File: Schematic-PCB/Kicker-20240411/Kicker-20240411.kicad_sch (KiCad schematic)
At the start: 21 parts, among them J1 Conn_01x02_Pin, J2 Conn_01x05_Pin, J3 Conn_01x02_Pin, Q1 NMOS, Q2 NMOS, U1 TSSP58P38, U2 TSSP58P38

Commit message: MD基板とキッカー基板を編集した
接続方法をピンヘッダ&ピンソケットに変更してみた
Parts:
- J2: footprint Connector_JST:JST_XH_S5B-XH-A-1_1x05_P2.50mm_Horizontal -> Connector_PinHeader_2.54mm:PinHeader_1x05_P2.54mm_Horizontal
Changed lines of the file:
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@@
 			)
 		)
-		(property "Footprint" "Connector_JST:JST_XH_S5B-XH-A-1_1x05_P2.50mm_Horizontal"
+		(property "Footprint" "Connector_PinHeader_2.54mm:PinHeader_1x05_P2.54mm_Horizontal"
 			(at 72.39 88.9 0)
 			(effects

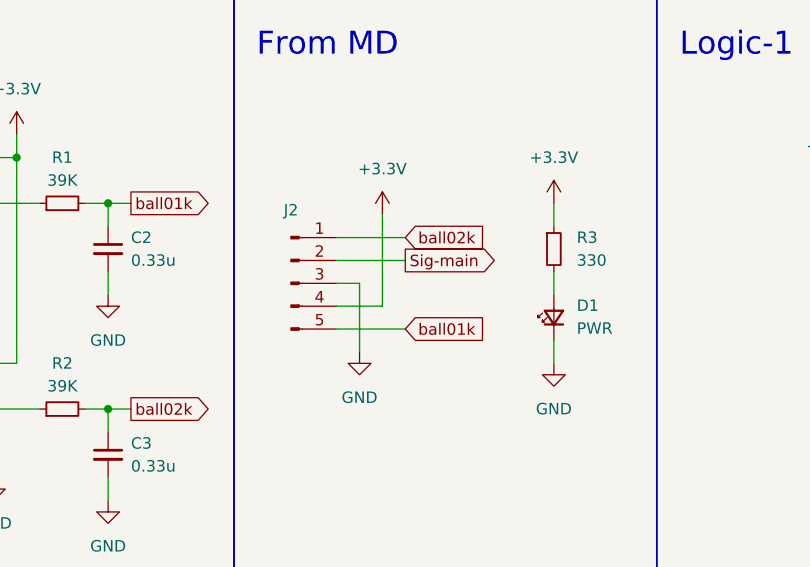
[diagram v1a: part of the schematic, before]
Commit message: 基板関連を編集した
MDとキッカーの融合基板のプロジェクト作成したから続きやっといてもらえるとありがたい
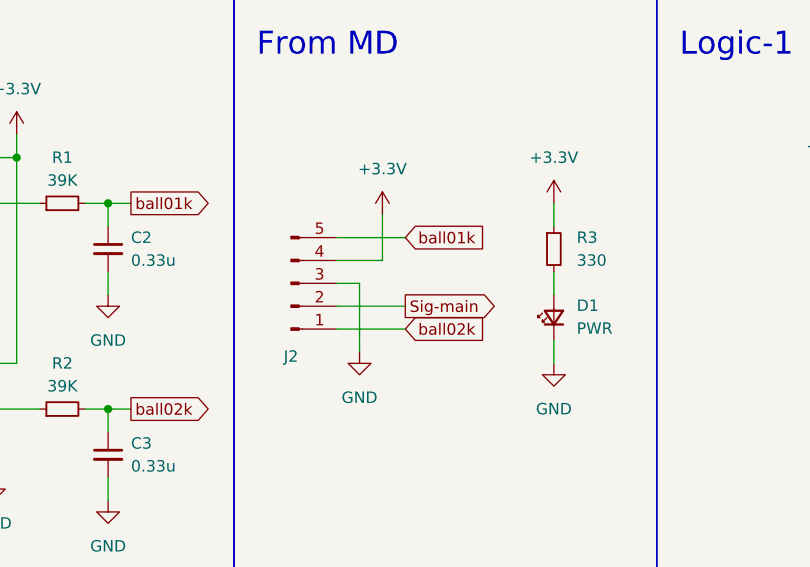
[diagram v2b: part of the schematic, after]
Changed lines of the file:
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@@
 	(wire
 		(pts
-			(xy 82.55 81.28) (xy 82.55 91.44)
-		)
-		(stroke
-			(width 0)
-			(type default)
-		)
-	)
-	(wire
-		(pts
 			(xy 119.38 40.64) (xy 119.38 43.18)
 		)
@@
 	(wire
 		(pts
+			(xy 82.55 86.36) (xy 82.55 81.28)
+		)
+		(stroke
+			(width 0)
+			(type default)
+		)
+	)
+	(wire
+		(pts
 			(xy 73.66 33.02) (xy 73.66 35.56)
 		)
@@
 	(wire
 		(pts
+			(xy 77.47 91.44) (xy 85.09 91.44)
+		)
+		(stroke
+			(width 0)
+			(type default)
+		)
+	)
+	(wire
+		(pts
 			(xy 93.98 35.56) (xy 96.52 35.56)
 		)
@@
 	(wire
 		(pts
+			(xy 77.47 86.36) (xy 82.55 86.36)
+		)
+		(stroke
+			(width 0)
+			(type default)
+		)
+	)
+	(wire
+		(pts
 			(xy 139.7 91.44) (xy 139.7 88.9)
 		)
@@
 	(wire
 		(pts
-			(xy 82.55 91.44) (xy 77.47 91.44)
-		)
-		(stroke
-			(width 0)
-			(type default)
-		)
-	)
-	(wire
-		(pts
 			(xy 175.26 88.9) (xy 177.8 88.9)
 		)
@@
 	(wire
 		(pts
-			(xy 77.47 86.36) (xy 85.09 86.36)
-		)
-		(stroke
-			(width 0)
-			(type default)
-		)
-	)
-	(wire
-		(pts
 			(xy 144.78 39.37) (xy 144.78 40.64)
 		)
@@
 	(global_label "ball02k"
 		(shape input)
-		(at 85.09 83.82 0)
+		(at 85.09 93.98 0)
 		(fields_autoplaced yes)
 		(effects
@@
 		)
 		(property "Intersheetrefs" "${INTERSHEET_REFS}"
-			(at 95.1507 83.82 0)
+			(at 95.1507 93.98 0)
 			(effects
 				(font
@@
 	(global_label "ball01k"
 		(shape input)
-		(at 85.09 93.98 0)
+		(at 85.09 83.82 0)
 		(fields_autoplaced yes)
 		(effects
@@
 		)
 		(property "Intersheetrefs" "${INTERSHEET_REFS}"
-			(at 95.1507 93.98 0)
+			(at 95.1507 83.82 0)
 			(effects
 				(font
@@
 	(global_label "Sig-main"
 		(shape output)
-		(at 85.09 86.36 0)
+		(at 85.09 91.44 0)
 		(fields_autoplaced yes)
 		(effects
@@
 		)
 		(property "Intersheetrefs" "${INTERSHEET_REFS}"
-			(at 105.531 86.36 0)
+			(at 105.531 91.44 0)
 			(effects
 				(font
@@
 		(lib_id "Connector:Conn_01x05_Pin")
 		(at 72.39 88.9 0)
+		(mirror x)
 		(unit 1)
 		(exclude_from_sim no)
@@
 		(dnp no)
 		(property "Reference" "J2"
-			(at 72.39 80.772 0)
+			(at 72.39 97.028 0)
 			(effects
 				(font
@@
 		)
 		(property "Value" "Conn_01x05_Pin"
-			(at 73.025 81.28 0)
+			(at 73.025 96.52 0)
 			(effects
 				(font

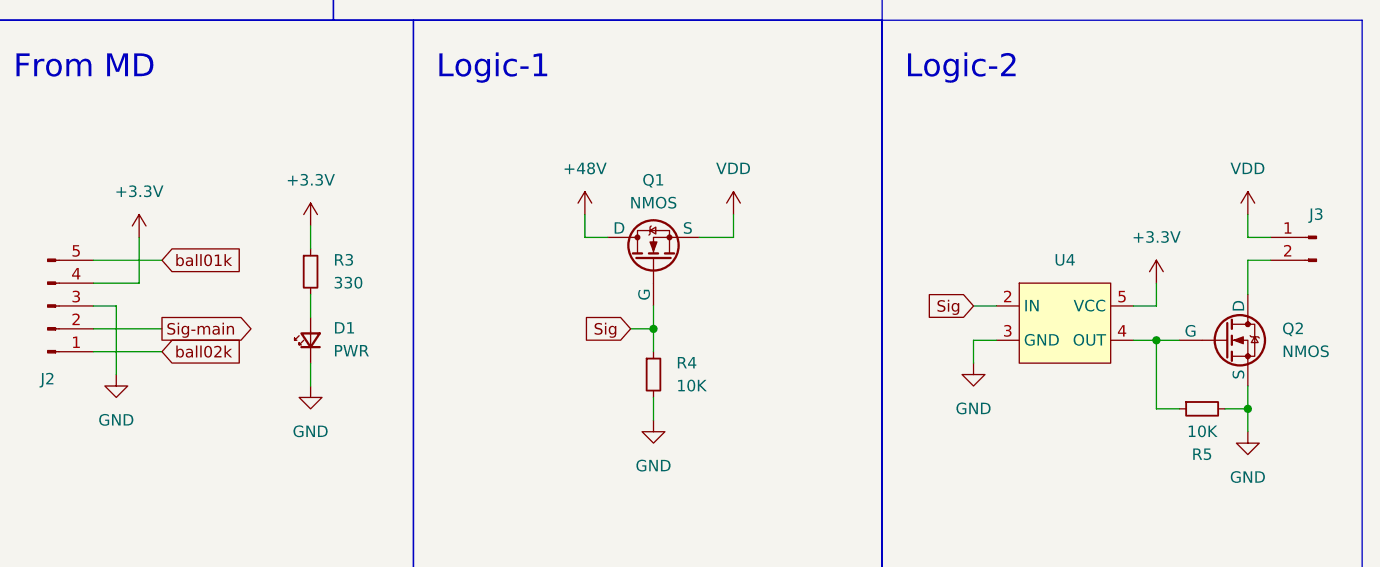
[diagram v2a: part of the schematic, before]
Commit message: キッカー基板を更新した
MDとの接続をピンヘッダ/ピンソケットを使う方式に変更した
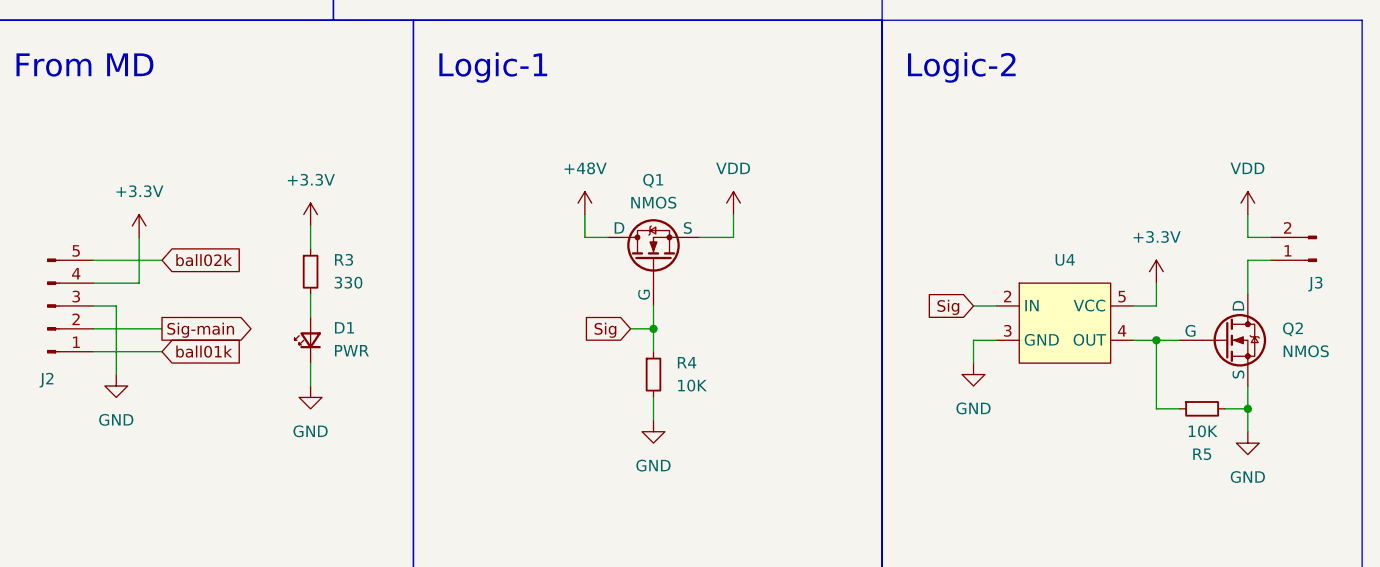
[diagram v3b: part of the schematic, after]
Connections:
- net VDD: now also J3.2 (Pin_2); no longer J3.1 (Pin_1)
- net ball01k: now also J2.1 (Pin_1); no longer J2.5 (Pin_5)
- net ball02k: now also J2.5 (Pin_5); no longer J2.1 (Pin_1)
- net at Q2.2 (D): now also J3.1 (Pin_1); no longer J3.2 (Pin_2)
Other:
- moved on the sheet: J3
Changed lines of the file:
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@@
 	(global_label "ball02k"
 		(shape input)
-		(at 85.09 93.98 0)
+		(at 85.09 83.82 0)
 		(fields_autoplaced yes)
 		(effects
@@
 		)
 		(property "Intersheetrefs" "${INTERSHEET_REFS}"
-			(at 95.1507 93.98 0)
+			(at 95.1507 83.82 0)
 			(effects
 				(font
@@
 	(global_label "ball01k"
 		(shape input)
-		(at 85.09 83.82 0)
+		(at 85.09 93.98 0)
 		(fields_autoplaced yes)
 		(effects
@@
 		)
 		(property "Intersheetrefs" "${INTERSHEET_REFS}"
-			(at 95.1507 83.82 0)
+			(at 95.1507 93.98 0)
 			(effects
 				(font
@@
 	(symbol
 		(lib_id "Connector:Conn_01x02_Pin")
-		(at 213.36 81.28 0)
-		(mirror y)
+		(at 213.36 83.82 180)
 		(unit 1)
 		(exclude_from_sim no)
@@
 		(dnp no)
 		(property "Reference" "J3"
-			(at 213.36 78.74 0)
+			(at 213.36 86.36 0)
 			(effects
 				(font
@@
 		)
 		(property "Value" "Conn_01x02_Pin"
-			(at 214.63 81.28 0)
+			(at 214.63 83.82 0)
 			(effects
 				(font
@@
 		)
 		(property "Footprint" "Connector_JST:JST_XH_S2B-XH-A-1_1x02_P2.50mm_Horizontal"
-			(at 213.36 81.28 0)
+			(at 213.36 83.82 0)
 			(effects
 				(font
@@
 		)
 		(property "Datasheet" "~"
-			(at 213.36 81.28 0)
+			(at 213.36 83.82 0)
 			(effects
 				(font
@@
 		)
 		(property "Description" "Generic connector, single row, 01x02, script generated"
-			(at 213.36 81.28 0)
-			(effects
-				(font
+			(at 213.36 83.82 0)
+			(effects
+				(font

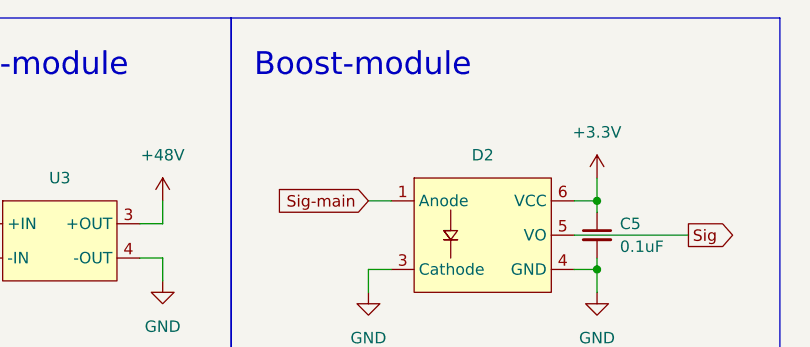
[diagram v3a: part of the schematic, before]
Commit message: フォトカプラの表記がBoost-moduleになっていたのを直した
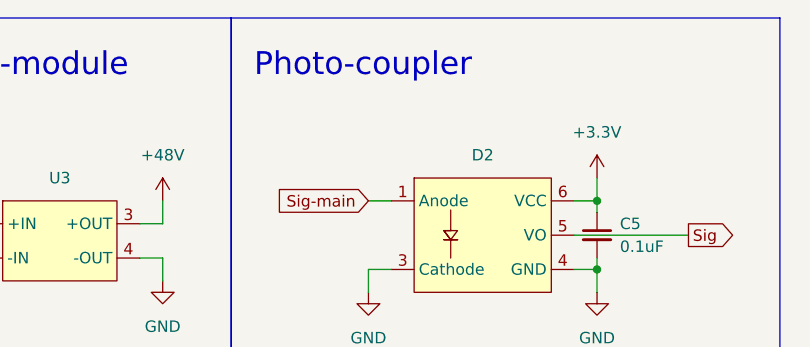
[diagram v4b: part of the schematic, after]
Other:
- note added: "Photo-coupler"
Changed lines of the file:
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@@
 		)
 	)
-	(text "Boost-module"
+	(text "Photo-coupler"
 		(exclude_from_sim no)
 		(at 106.68 16.51 0)

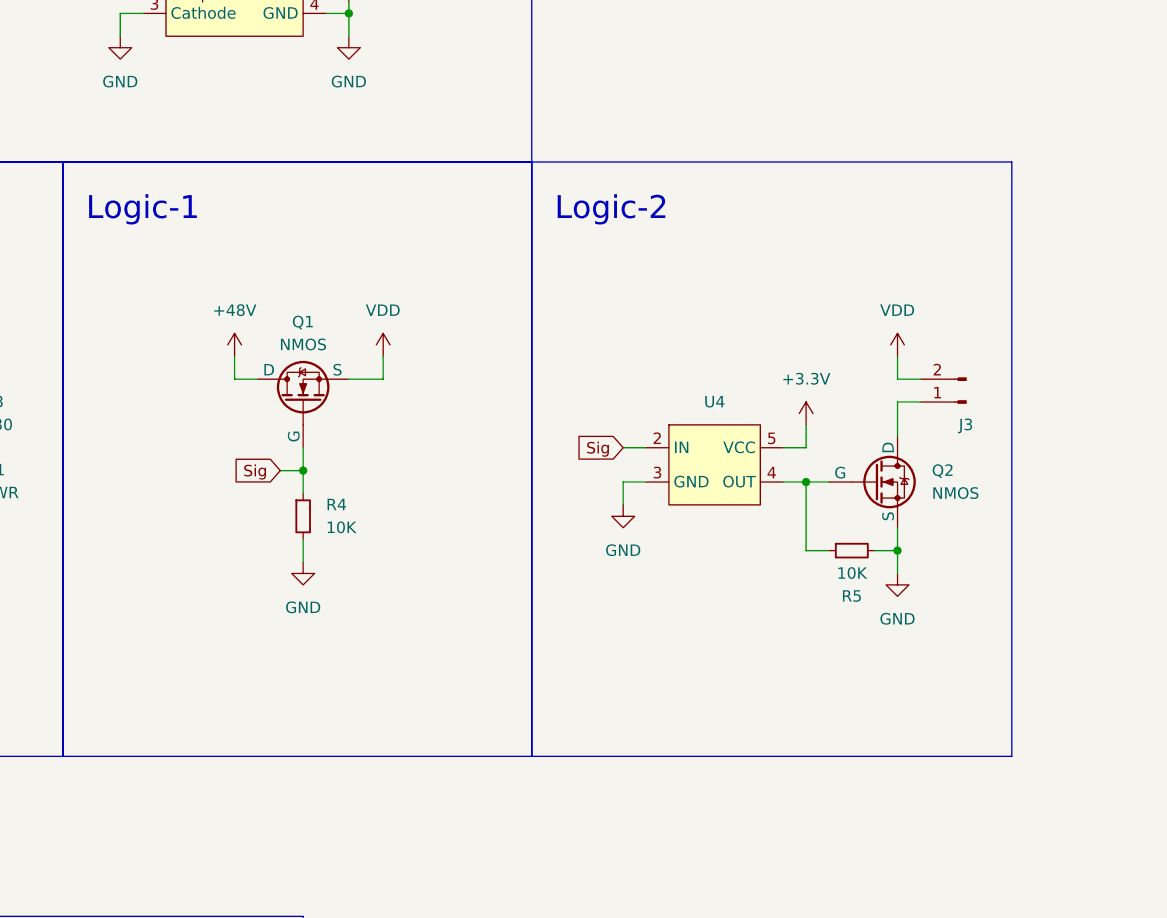
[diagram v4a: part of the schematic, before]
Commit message: キッカー基板更新した
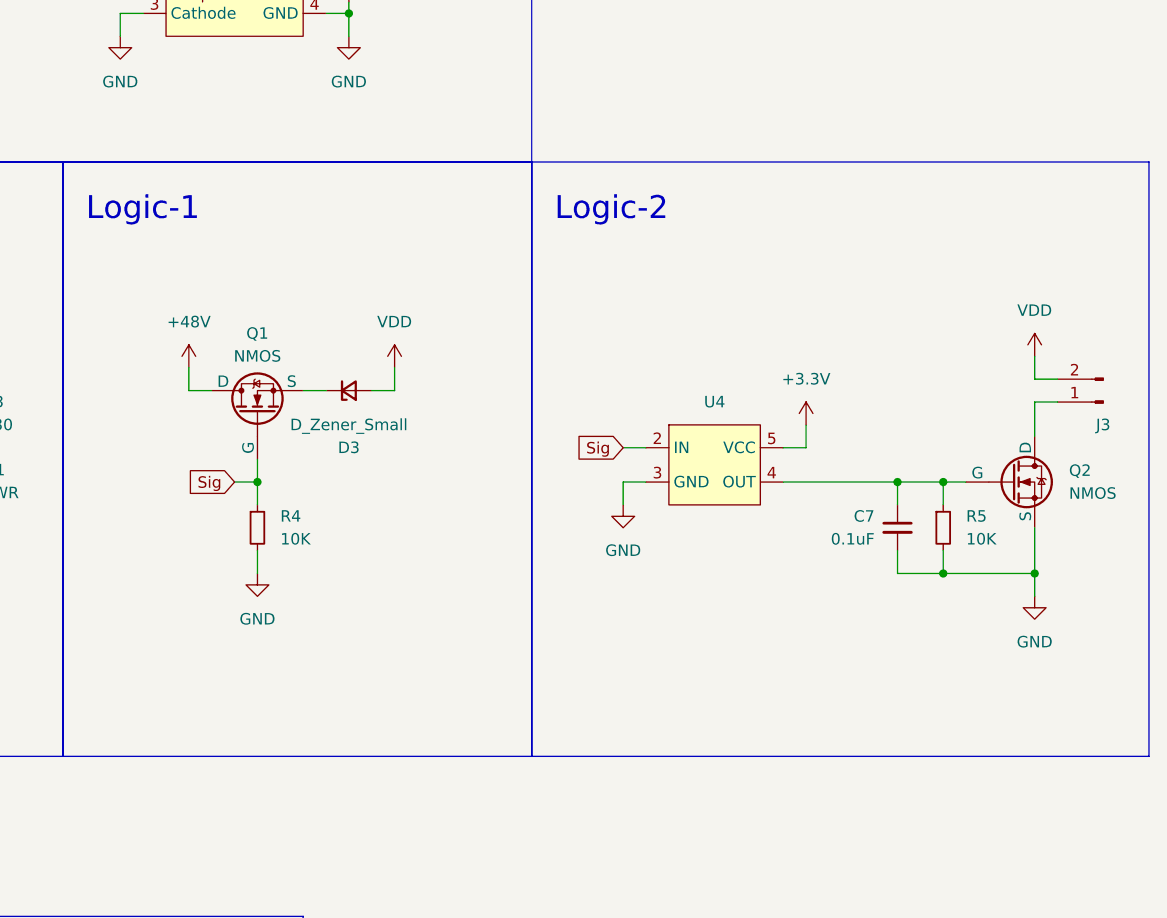
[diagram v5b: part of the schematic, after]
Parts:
- added C7: 0.1uF, Capacitor_SMD:C_0603_1608Metric, symbol Device:C_Small
- added D3: D_Zener_Small, symbol Device:D_Zener_Small
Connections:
- net GND: now also C7.2
- net VDD: now also D3.2 (A); no longer Q1.3 (S)
- net at Q2.1 (G), R5.1, U4.4 (OUT): now also C7.1
- new net: D3.1 (K), Q1.3 (S)
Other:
- moved on the sheet: J3, Q1, Q2, R4
